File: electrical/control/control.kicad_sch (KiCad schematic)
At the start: 46 parts, among them J1 USB4105-GF-A, J3 SM03B-SRSS-TB, J4 SM04B-SRSS-TB, J5 TC2030-NL, J6 SM03B-SRSS-TB, SW1 BOOT, U1 RP2040, U2 ABPMRRV001PD2A3, U4 W25Q16JVSSIQ, U5 LP5907MFX-3.3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

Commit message: ERC fix and minor cleanup
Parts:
- R1, R2, R7: value 5.1k -> 5k1
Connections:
- net SWD is gone; now on net SWDIO: J3.3 (SD)
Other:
- company: (none) -> Bushel Basket Musical Instruments
- title: (none) -> MIDI Concertina Controller
- moved on the sheet: C2, C3, R5
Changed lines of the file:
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@@
 	(generator_version "9.0")
 	(paper "USLedger")
+	(title_block
+		(title "MIDI Concertina Controller")
+		(company "Bushel Basket Musical Instruments")
+	)
 	(junction
 		(at 92.71 113.03)
@@
 	)
 	(junction
-		(at 49.53 252.73)
+		(at 49.53 250.19)
 		(diameter 0)
 		(color 0 0 0 0)
@@
 	)
 	(junction
-		(at 49.53 224.79)
+		(at 49.53 227.33)
 		(diameter 0)
 		(color 0 0 0 0)
@@
 	)
 	(junction
-		(at 26.67 252.73)
+		(at 24.13 250.19)
 		(diameter 0)
 		(color 0 0 0 0)
@@
 	(wire
 		(pts
-			(xy 67.31 252.73) (xy 72.39 252.73)
+			(xy 67.31 250.19) (xy 72.39 250.19)
 		)
 		(stroke
@@
 	(wire
 		(pts
-			(xy 49.53 224.79) (xy 72.39 224.79)
+			(xy 49.53 227.33) (xy 72.39 227.33)
 		)
 		(stroke
@@
 	(wire
 		(pts
-			(xy 26.67 252.73) (xy 31.75 252.73)
+			(xy 24.13 250.19) (xy 31.75 250.19)
 		)
 		(stroke
@@
 	(wire
 		(pts
-			(xy 26.67 255.27) (xy 26.67 252.73)
+			(xy 24.13 252.73) (xy 24.13 250.19)
 		)
 		(stroke
@@
 	(wire
 		(pts
-			(xy 39.37 224.79) (xy 49.53 224.79)
+			(xy 39.37 227.33) (xy 49.53 227.33)
 		)
 		(stroke
@@
 	(wire
 		(pts
-			(xy 49.53 242.57) (xy 49.53 252.73)
+			(xy 49.53 242.57) (xy 49.53 250.19)
 		)
 		(stroke
@@
 	(wire
 		(pts
-			(xy 44.45 153.67) (xy 46.99 153.67)
-		)
-		(stroke
-			(width 0)
-			(type default)
-		)
-	)
-	(wire
-		(pts
 			(xy 123.19 49.53) (xy 123.19 46.99)
 		)
@@
 	(wire
 		(pts
-			(xy 39.37 252.73) (xy 49.53 252.73)
+			(xy 39.37 250.19) (xy 49.53 250.19)
 		)
 		(stroke
@@
 	(wire
 		(pts
-			(xy 26.67 252.73) (xy 26.67 224.79)
+			(xy 24.13 250.19) (xy 24.13 227.33)
 		)
 		(stroke
@@
 	(wire
 		(pts
-			(xy 49.53 224.79) (xy 49.53 234.95)
+			(xy 49.53 227.33) (xy 49.53 234.95)
 		)
 		(stroke
@@
 	(wire
 		(pts
-			(xy 49.53 252.73) (xy 59.69 252.73)
+			(xy 49.53 250.19) (xy 59.69 250.19)
 		)
 		(stroke
@@
 	(wire
 		(pts
-			(xy 26.67 224.79) (xy 31.75 224.79)
+			(xy 24.13 227.33) (xy 31.75 227.33)
 		)
 		(stroke
@@
 	(global_label "XIN"
 		(shape passive)
-		(at 72.39 224.79 0)
+		(at 72.39 227.33 0)
 		(fields_autoplaced yes)
 		(effects
@@
 		)
 		(property "Intersheetrefs" "${INTERSHEET_REFS}"
-			(at 77.4087 224.79 0)
+			(at 77.4087 227.33 0)
 			(effects
 				(font
@@
 		)
 	)
-	(global_label "SWD"
+	(global_label "SWDIO"
 		(shape bidirectional)
 		(at 124.46 233.68 0)
@@
 		)
 		(property "Intersheetrefs" "${INTERSHEET_REFS}"
-			(at 132.4874 233.68 0)
+			(at 134.4227 233.68 0)
 			(effects
 				(font
@@
 	(global_label "XOUT"
 		(shape passive)
-		(at 72.39 252.73 0)
+		(at 72.39 250.19 0)
 		(fields_autoplaced yes)
 		(effects
@@
 		)
 		(property "Intersheetrefs" "${INTERSHEET_REFS}"
-			(at 79.102 252.73 0)
+			(at 79.102 250.19 0)
 			(effects
 				(font
@@
 	(symbol
 		(lib_id "Device:R_US")
-		(at 63.5 252.73 90)
+		(at 63.5 250.19 90)
 		(unit 1)
 		(exclude_from_sim no)
@@
 		(dnp no)
 		(property "Reference" "R5"
-			(at 63.5 246.38 90)
+			(at 63.5 243.84 90)
 			(effects
 				(font
@@
 		)
 		(property "Value" "1k"
-			(at 63.5 248.92 90)
+			(at 63.5 246.38 90)
 			(effects
 				(font
@@
 		)
 		(property "Footprint" "Resistor_SMD:R_0402_1005Metric"
-			(at 63.754 251.714 90)
+			(at 63.754 249.174 90)
 			(effects
 				(font
@@
 		)
 		(property "Datasheet" "~"
-			(at 63.5 252.73 0)
+			(at 63.5 250.19 0)
 			(effects
 				(font
@@
 		)
 		(property "Description" "Resistor, US symbol"
-			(at 63.5 252.73 0)
+			(at 63.5 250.19 0)
 			(effects
 				(font
@@
 		)
 		(property "Tolerance" "1%"
-			(at 63.5 256.54 90)
+			(at 63.5 254 90)
 			(effects
 				(font
@@
 	(symbol
 		(lib_id "Device:C")
-		(at 35.56 224.79 90)
+		(at 35.56 227.33 90)
 		(unit 1)
 		(exclude_from_sim no)
@@
 		(dnp no)
 		(property "Reference" "C3"
-			(at 35.56 218.44 90)
+			(at 35.56 220.98 90)
 			(effects
 				(font
@@
 		)
 		(property "Value" "15p"
-			(at 35.56 220.98 90)
+			(at 35.56 223.52 90)
 			(effects
 				(font
@@
 		)
 		(property "Footprint" "Capacitor_SMD:C_0402_1005Metric"
-			(at 39.37 223.8248 0)
+			(at 39.37 226.3648 0)
 			(effects
 				(font
@@
 		)
 		(property "Datasheet" "~"
-			(at 35.56 224.79 0)
+			(at 35.56 227.33 0)
 			(effects
 				(font
@@
 		)
 		(property "Description" "Unpolarized capacitor"
-			(at 35.56 224.79 0)
+			(at 35.56 227.33 0)
 			(effects
 				(font
@@
 			)
 		)
-		(property "Value" "5.1k"
+		(property "Value" "5k1"
 			(at 95.25 105.4099 0)
 			(effects
@@
 			)
 		)
-		(property "Value" "5.1k"
+		(property "Value" "5k1"
 			(at 87.63 52.0699 0)
 			(effects
@@
 	(symbol
 		(lib_id "Device:C")
-		(at 35.56 252.73 90)
+		(at 35.56 250.19 90)
 		(unit 1)
 		(exclude_from_sim no)
@@
 		(dnp no)
 		(property "Reference" "C2"
-			(at 35.56 246.38 90)
+			(at 35.56 243.84 90)
 			(effects
 				(font
@@
 		)
 		(property "Value" "15p"
-			(at 35.56 248.92 90)
+			(at 35.56 246.38 90)
 			(effects
 				(font
@@
 		)
 		(property "Footprint" "Capacitor_SMD:C_0402_1005Metric"
-			(at 39.37 251.7648 0)
+			(at 39.37 249.2248 0)
 			(effects
 				(font
@@
 		)
 		(property "Datasheet" "~"
-			(at 35.56 252.73 0)
+			(at 35.56 250.19 0)
 			(effects
 				(font
@@
 		)
 		(property "Description" "Unpolarized capacitor"
-			(at 35.56 252.73 0)
+			(at 35.56 250.19 0)
 			(effects
 				(font
@@
 	(symbol
 		(lib_id "power:GND")
-		(at 26.67 255.27 0)
+		(at 24.13 252.73 0)
 		(unit 1)
 		(exclude_from_sim no)
@@
 		(fields_autoplaced yes)
 		(property "Reference" "#PWR015"
-			(at 26.67 261.62 0)
+			(at 24.13 259.08 0)
 			(effects
 				(font
@@
 		)
 		(property "Value" "GND"
-			(at 26.67 260.35 0)
+			(at 24.13 257.81 0)
 			(effects
 				(font
@@
 		)
 		(property "Footprint" ""
-			(at 26.67 255.27 0)
+			(at 24.13 252.73 0)
 			(effects
 				(font
@@
 		)
 		(property "Datasheet" ""
-			(at 26.67 255.27 0)
+			(at 24.13 252.73 0)
 			(effects
 				(font
@@
 		)
 		(property "Description" "Power symbol creates a global label with name \"GND\" , ground"
-			(at 26.67 255.27 0)
+			(at 24.13 252.73 0)
 			(effects
 				(font
@@
 	(symbol
 		(lib_id "power:GND")
-		(at 46.99 153.67 0)
+		(at 44.45 153.67 0)
 		(unit 1)
 		(exclude_from_sim no)
@@
 		(fields_autoplaced yes)
 		(property "Reference" "#PWR07"
-			(at 46.99 160.02 0)
+			(at 44.45 160.02 0)
 			(effects
 				(font
@@
 		)
 		(property "Value" "GND"
-			(at 46.99 158.75 0)
+			(at 44.45 158.75 0)
 			(effects
 				(font
@@
 		)
 		(property "Footprint" ""
-			(at 46.99 153.67 0)
+			(at 44.45 153.67 0)
 			(effects
 				(font
@@
 		)
 		(property "Datasheet" ""
-			(at 46.99 153.67 0)
+			(at 44.45 153.67 0)
 			(effects
 				(font
@@
 		)
 		(property "Description" "Power symbol creates a global label with name \"GND\" , ground"
-			(at 46.99 153.67 0)
+			(at 44.45 153.67 0)
 			(effects
 				(font
@@
 			)
 		)
-		(property "Value" "5.1k"
+		(property "Value" "5k1"
 			(at 77.47 52.0699 0)
 			(effects

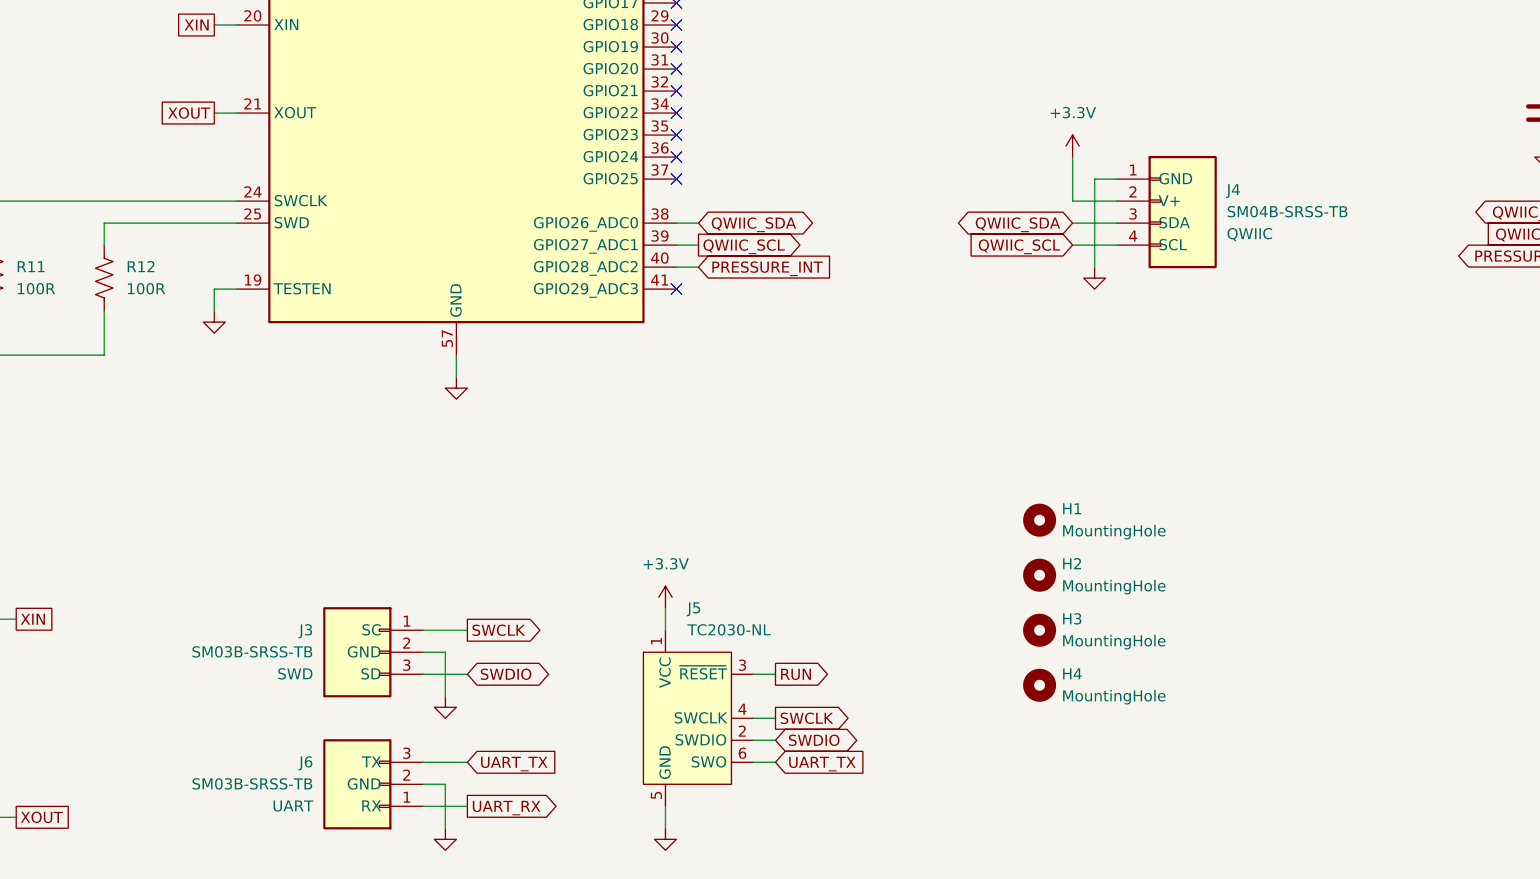
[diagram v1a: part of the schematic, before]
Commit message: Use standard symbols and footprints for connectors
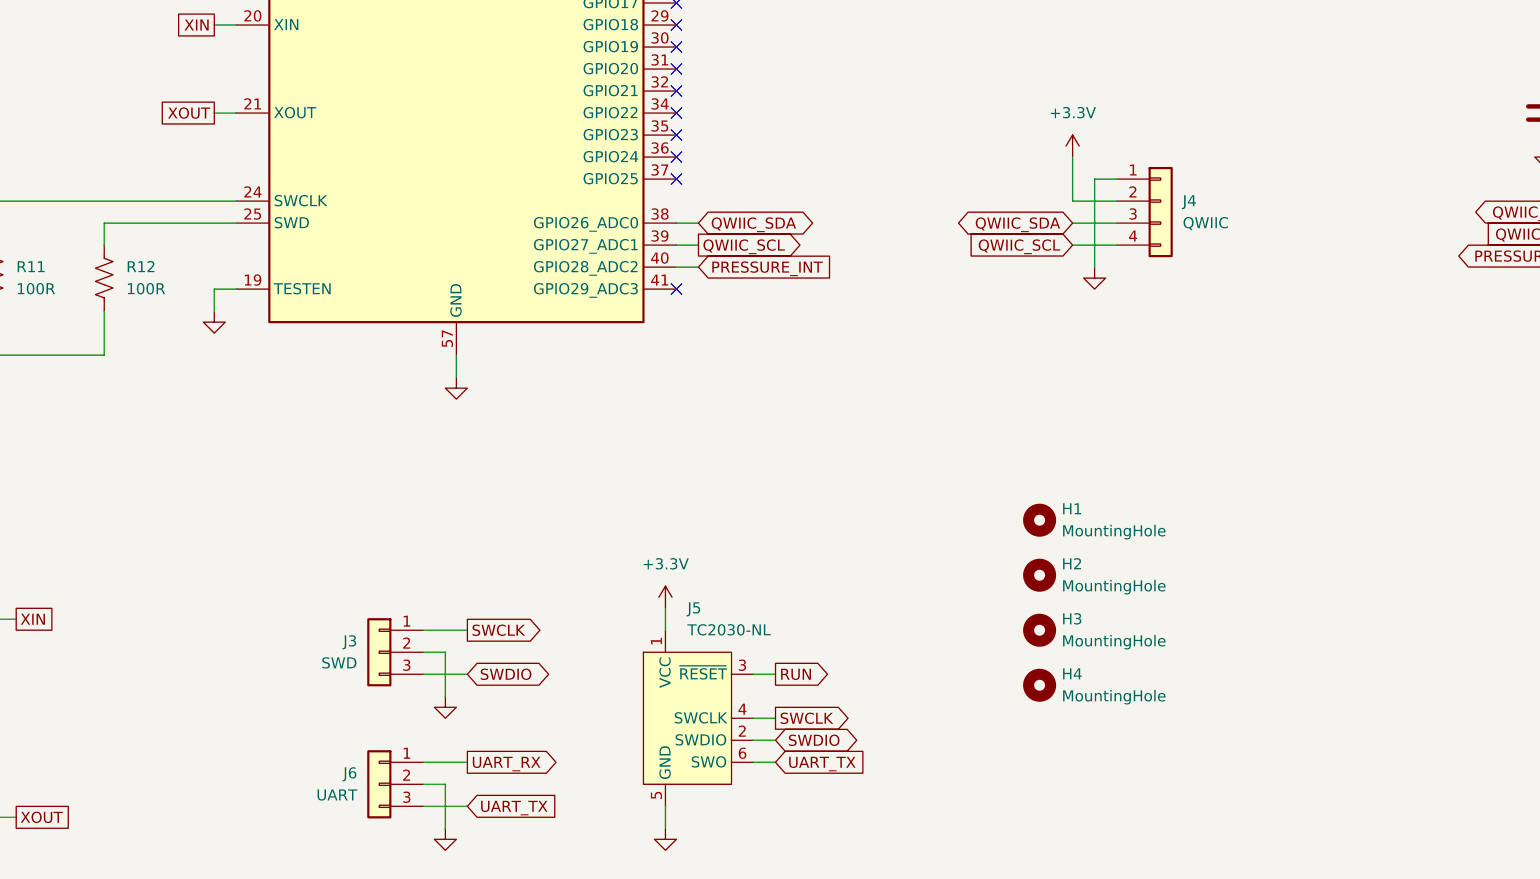
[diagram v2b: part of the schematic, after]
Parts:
- J3: value SM03B-SRSS-TB -> SWD; footprint (none) -> Connector_JST:JST_SH_SM03B-SRSS-TB_1x03-1MP_P1.00mm_Horizontal; Label SWD -> (none)
- J4: value SM04B-SRSS-TB -> QWIIC; footprint (none) -> Connector_JST:JST_SH_SM04B-SRSS-TB_1x04-1MP_P1.00mm_Horizontal; Label QWIIC -> (none)
- J6: value SM03B-SRSS-TB -> UART; footprint (none) -> Connector_JST:JST_SH_SM03B-SRSS-TB_1x03-1MP_P1.00mm_Horizontal; Label UART -> (none)
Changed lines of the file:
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@@
 	(wire
 		(pts
-			(xy 119.38 248.92) (xy 124.46 248.92)
+			(xy 119.38 243.84) (xy 124.46 243.84)
 		)
 		(stroke
@@
 	(wire
 		(pts
-			(xy 119.38 243.84) (xy 124.46 243.84)
+			(xy 119.38 248.92) (xy 124.46 248.92)
 		)
 		(stroke
@@
 	(global_label "UART_TX"
 		(shape input)
-		(at 124.46 243.84 0)
+		(at 124.46 248.92 0)
 		(fields_autoplaced yes)
 		(effects
@@
 		)
 		(property "Intersheetrefs" "${INTERSHEET_REFS}"
-			(at 135.2466 243.84 0)
+			(at 135.2466 248.92 0)
 			(effects
 				(font
@@
 	(global_label "UART_RX"
 		(shape output)
-		(at 124.46 248.92 0)
+		(at 124.46 243.84 0)
 		(fields_autoplaced yes)
 		(effects
@@
 		)
 		(property "Intersheetrefs" "${INTERSHEET_REFS}"
-			(at 135.549 248.92 0)
+			(at 135.549 243.84 0)
 			(effects
 				(font
@@
 	(symbol
 		(lib_id "Connector_Generic:Conn_01x03")
-		(at 111.76 231.14 0)
+		(at 114.3 231.14 0)
 		(mirror y)
 		(unit 1)
@@
 		(dnp no)
 		(property "Reference" "J3"
-			(at 106.68 228.6 0)
+			(at 111.76 229.87 0)
 			(effects
 				(font
@@
 			)
 		)
-		(property "Value" "SM03B-SRSS-TB"
-			(at 106.68 231.14 0)
+		(property "Value" "SWD"
+			(at 111.76 232.41 0)
 			(effects
 				(font
@@
 			)
 		)
-		(property "Footprint" ""
-			(at 111.76 231.14 0)
+		(property "Footprint" "Connector_JST:JST_SH_SM03B-SRSS-TB_1x03-1MP_P1.00mm_Horizontal"
+			(at 114.3 231.14 0)
 			(effects
 				(font
@@
 		)
 		(property "Datasheet" "~"
-			(at 111.76 231.14 0)
+			(at 114.3 231.14 0)
 			(effects
 				(font
@@
 		)
 		(property "Description" "Generic connector, single row, 01x03, script generated (kicad-library-utils/schlib/autogen/connector/)"
-			(at 111.76 231.14 0)
+			(at 114.3 231.14 0)
 			(effects
 				(font
@@
 			)
 		)
-		(property "Label" "SWD"
-			(at 106.68 233.68 0)
-			(effects
-				(font
-					(size 1.27 1.27)
-				)
-				(justify left)
-			)
-		)
 		(pin "1"
 		)
@@
 	)
 	(symbol
-		(lib_name "Conn_01x04_1")
 		(lib_id "Connector_Generic:Conn_01x04")
-		(at 207.01 179.07 0)
+		(at 204.47 179.07 0)
 		(unit 1)
 		(exclude_from_sim no)
@@
 		(dnp no)
 		(property "Reference" "J4"
-			(at 212.09 177.8 0)
+			(at 207.01 179.07 0)
 			(effects
 				(font
@@
 			)
 		)
-		(property "Value" "SM04B-SRSS-TB"
-			(at 212.09 180.34 0)
+		(property "Value" "QWIIC"
+			(at 207.01 181.61 0)
 			(effects
 				(font
@@
 			)
 		)
-		(property "Footprint" ""
-			(at 207.01 179.07 0)
+		(property "Footprint" "Connector_JST:JST_SH_SM04B-SRSS-TB_1x04-1MP_P1.00mm_Horizontal"
+			(at 204.47 179.07 0)
 			(effects
 				(font
@@
 		)
 		(property "Datasheet" "~"
-			(at 207.01 179.07 0)
+			(at 204.47 179.07 0)
 			(effects
 				(font
@@
 		)
 		(property "Description" "Generic connector, single row, 01x04, script generated (kicad-library-utils/schlib/autogen/connector/)"
-			(at 207.01 179.07 0)
+			(at 204.47 179.07 0)
 			(effects
 				(font
@@
 			)
 		)
-		(property "Label" "QWIIC"
-			(at 212.09 182.88 0)
-			(effects
-				(font
-					(size 1.27 1.27)
-				)
-				(justify left)
-			)
-		)
 		(pin "3"
 		)
@@
 	)
 	(symbol
-		(lib_name "Conn_01x03_1")
 		(lib_id "Connector_Generic:Conn_01x03")
-		(at 111.76 246.38 180)
+		(at 114.3 246.38 0)
+		(mirror y)
 		(unit 1)
 		(exclude_from_sim no)
@@
 		(dnp no)
 		(property "Reference" "J6"
-			(at 106.68 243.84 0)
+			(at 111.76 245.11 0)
 			(effects
 				(font
@@
 			)
 		)
-		(property "Value" "SM03B-SRSS-TB"
-			(at 106.68 246.38 0)
+		(property "Value" "UART"
+			(at 111.76 247.65 0)
 			(effects
 				(font
@@
 			)
 		)
-		(property "Footprint" ""
-			(at 111.76 246.38 0)
+		(property "Footprint" "Connector_JST:JST_SH_SM03B-SRSS-TB_1x03-1MP_P1.00mm_Horizontal"
+			(at 114.3 246.38 0)
 			(effects
 				(font
@@
 		)
 		(property "Datasheet" "~"
-			(at 111.76 246.38 0)
+			(at 114.3 246.38 0)
 			(effects
 				(font
@@
 		)
 		(property "Description" "Generic connector, single row, 01x03, script generated (kicad-library-utils/schlib/autogen/connector/)"
-			(at 111.76 246.38 0)
+			(at 114.3 246.38 0)
 			(effects
 				(font
@@
 			)
 		)
-		(property "Label" "UART"
-			(at 106.68 248.92 0)
-			(effects
-				(font
-					(size 1.27 1.27)
-				)
-				(justify left)
-			)
-		)
